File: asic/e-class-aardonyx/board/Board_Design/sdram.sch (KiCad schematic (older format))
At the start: 30 parts, among them J4 Conn_1x4, U15 SKT32E, U2 IS42S32160F-TSOP2, U3 CDCE913PW, Y2 27MHz

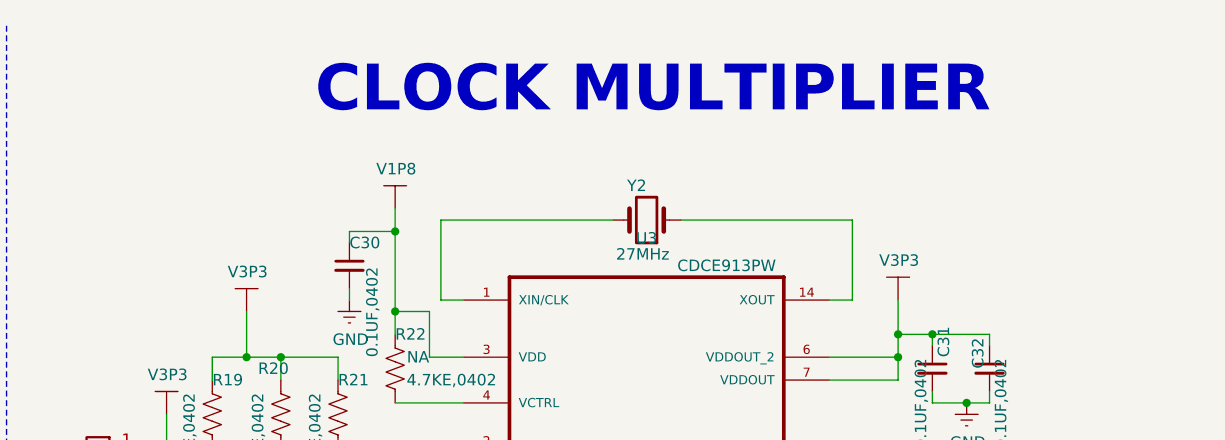
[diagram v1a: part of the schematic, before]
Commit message: Adding capacitors to clock
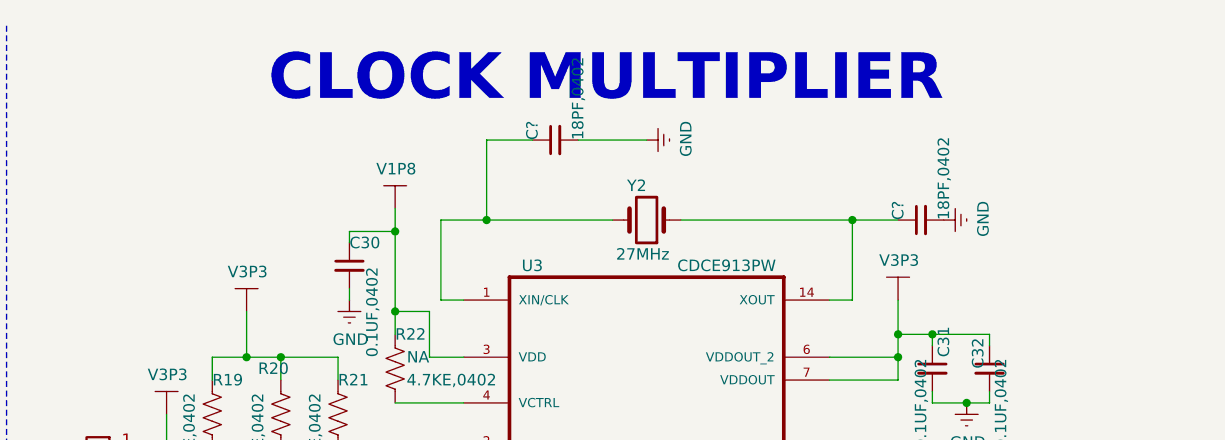
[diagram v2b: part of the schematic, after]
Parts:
- added C? (x2): 18PF,0402, Capacitor_SMD:C_0402_1005Metric, symbol Aardonyx-rescue:C_Small-aardonyx
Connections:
- net GNDREF: now also C?.2, C?.2
- net at U3.1 (XIN/CLK), Y2.2: now also C?.1
- net at U3.14 (XOUT), Y2.1: now also C?.1
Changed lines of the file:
@@
 Text Label 10200 2600 0    50   ~ 0
 CLK
-Text Notes 7300 900  0    200  ~ 40
+Text Notes 10050 850  2    200  ~ 40
 CLOCK MULTIPLIER\n
 Wire Wire Line
-	8600 1350 7850 1350
+	8600 1350 8050 1350
 Wire Wire Line
 	7850 1350 7850 1700
@@
 AR Path="/5ED5EB9F" Ref="U3"  Part="1"
 AR Path="/5D8B37B8/5ED5EB9F" Ref="U3"  Part="1"
-F 0 "U3" H 8750 2970 50  0000 C CNN
+F 0 "U3" H 8250 2850 50  0000 C CNN
 F 1 "CDCE913PW" H 9100 2850 50  0000 C CNN
 F 2 "Package_SO:TSSOP-14_4.4x5mm_P0.65mm" H 8900 2000 50  0001 L BNN
@@
 	7650 1400 7650 1300
 Connection ~ 7650 1400
+$Comp
+L Aardonyx-rescue:C_Small-aardonyx C?
+U 1 1 5F202590
+P 9950 1350
+F 0 "C?" H 9950 1450 50  0000 L CNN
+F 1 "18PF,0402" H 9950 1250 50  0000 L CNN
+F 2 "Capacitor_SMD:C_0402_1005Metric" H 9950 1350 50  0001 C CNN
+F 3 "https://www.digikey.in/product-detail/en/yageo/CC0201JRNPO9BN180/311-1386-1-ND/2833692" H 9950 1350 50  0001 C CNN
+F 4 "311-1386-1-ND " H 9950 1350 50  0001 C CNN "Digikey PartNumber"
+F 5 "CAP CER 18PF 50V C0G/NPO 0201 " H 9950 1350 50  0001 C CNN "Description"
+F 6 "CC0201JRNPO9BN180 " H 9950 1350 50  0001 C CNN "Manufactured Part Number"
+F 7 "Yageo" H 9950 1350 50  0001 C CNN "Maufaturer"
+	1    9950 1350
+	0    -1   -1   0
+$EndComp
+Wire Wire Line
+	9850 1350 9650 1350
+Connection ~ 9650 1350
+$Comp
+L Aardonyx-rescue:GND-aardonyx #PWR?
+U 1 1 5F21B9C6
+P 10050 1350
+AR Path="/5D8B3740/5F21B9C6" Ref="#PWR?"  Part="1"
+AR Path="/5D8B37B8/5F21B9C6" Ref="#PWR?"  Part="1"
+F 0 "#PWR?" H 10050 1100 50  0001 C CNN
+F 1 "GND" H 10055 1177 50  0000 C CNN
+F 2 "" H 10050 1350 50  0001 C CNN
+F 3 "" H 10050 1350 50  0001 C CNN
+	1    10050 1350
+	0    -1   -1   0
+$EndComp
+$Comp
+L Aardonyx-rescue:C_Small-aardonyx C?
+U 1 1 5F229012
+P 8350 1000
+F 0 "C?" H 8350 1100 50  0000 L CNN
+F 1 "18PF,0402" H 8350 900 50  0000 L CNN
+F 2 "Capacitor_SMD:C_0402_1005Metric" H 8350 1000 50  0001 C CNN
+F 3 "https://www.digikey.in/product-detail/en/yageo/CC0201JRNPO9BN180/311-1386-1-ND/2833692" H 8350 1000 50  0001 C CNN
+F 4 "311-1386-1-ND " H 8350 1000 50  0001 C CNN "Digikey PartNumber"
+F 5 "CAP CER 18PF 50V C0G/NPO 0201 " H 8350 1000 50  0001 C CNN "Description"
+F 6 "CC0201JRNPO9BN180 " H 8350 1000 50  0001 C CNN "Manufactured Part Number"
+F 7 "Yageo" H 8350 1000 50  0001 C CNN "Maufaturer"
+	1    8350 1000
+	0    -1   -1   0
+$EndComp
+Wire Wire Line
+	8250 1000 8050 1000
+Wire Wire Line
+	8750 1000 8450 1000
+$Comp
+L Aardonyx-rescue:GND-aardonyx #PWR?
+U 1 1 5F24315B
+P 8750 1000
+AR Path="/5D8B3740/5F24315B" Ref="#PWR?"  Part="1"
+AR Path="/5D8B37B8/5F24315B" Ref="#PWR?"  Part="1"
+F 0 "#PWR?" H 8750 750 50  0001 C CNN
+F 1 "GND" H 8755 827 50  0000 C CNN
+F 2 "" H 8750 1000 50  0001 C CNN
+F 3 "" H 8750 1000 50  0001 C CNN
+	1    8750 1000
+	0    -1   -1   0
+$EndComp
+Wire Wire Line
+	8050 1000 8050 1350
 Wire Bus Line
 	1550 5700 1550 6100
@@
 Wire Bus Line
 	4650 3000 4650 6600
+Connection ~ 8050 1350
+Wire Wire Line
+	8050 1350 7850 1350
 $EndSCHEMATC

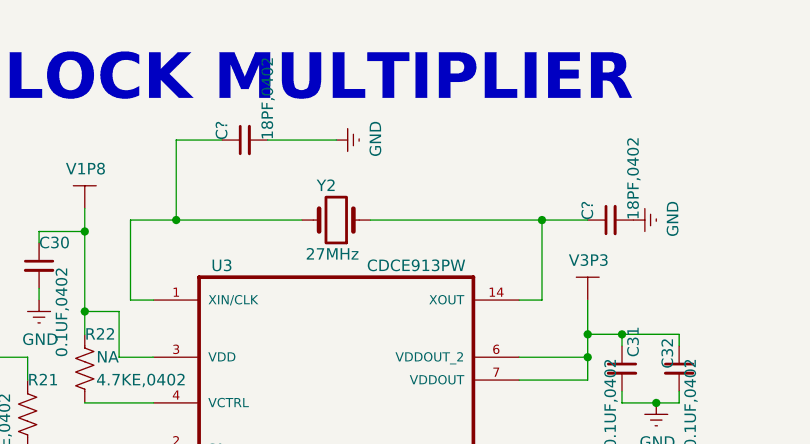
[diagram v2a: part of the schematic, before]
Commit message: updated footprint c37 & f1
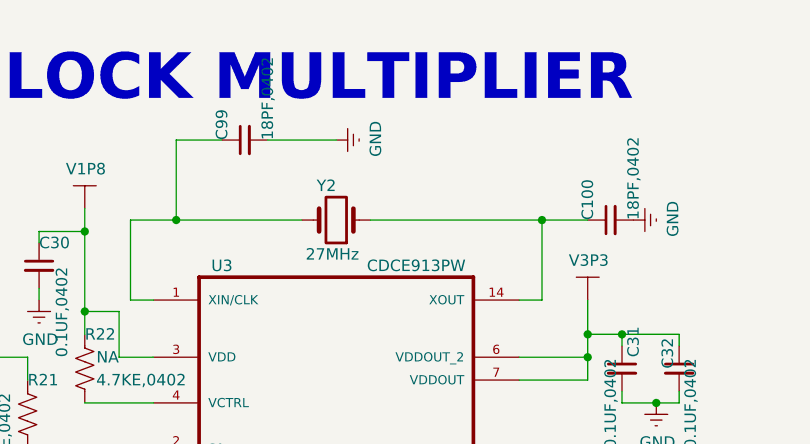
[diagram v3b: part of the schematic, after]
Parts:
- gave numbers to parts that had none: 2
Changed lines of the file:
@@
 Connection ~ 7650 1400
 $Comp
-L Aardonyx-rescue:C_Small-aardonyx C?
+L Aardonyx-rescue:C_Small-aardonyx C100
 U 1 1 5F202590
 P 9950 1350
-F 0 "C?" H 9950 1450 50  0000 L CNN
+F 0 "C100" H 9950 1450 50  0000 L CNN
 F 1 "18PF,0402" H 9950 1250 50  0000 L CNN
 F 2 "Capacitor_SMD:C_0402_1005Metric" H 9950 1350 50  0001 C CNN
@@
 P 10050 1350
 AR Path="/5D8B3740/5F21B9C6" Ref="#PWR?"  Part="1"
-AR Path="/5D8B37B8/5F21B9C6" Ref="#PWR?"  Part="1"
-F 0 "#PWR?" H 10050 1100 50  0001 C CNN
+AR Path="/5D8B37B8/5F21B9C6" Ref="#PWR0186"  Part="1"
+F 0 "#PWR0186" H 10050 1100 50  0001 C CNN
 F 1 "GND" H 10055 1177 50  0000 C CNN
 F 2 "" H 10050 1350 50  0001 C CNN
@@
 $EndComp
 $Comp
-L Aardonyx-rescue:C_Small-aardonyx C?
+L Aardonyx-rescue:C_Small-aardonyx C99
 U 1 1 5F229012
 P 8350 1000
-F 0 "C?" H 8350 1100 50  0000 L CNN
+F 0 "C99" H 8350 1100 50  0000 L CNN
 F 1 "18PF,0402" H 8350 900 50  0000 L CNN
 F 2 "Capacitor_SMD:C_0402_1005Metric" H 8350 1000 50  0001 C CNN
@@
 P 8750 1000
 AR Path="/5D8B3740/5F24315B" Ref="#PWR?"  Part="1"
-AR Path="/5D8B37B8/5F24315B" Ref="#PWR?"  Part="1"
-F 0 "#PWR?" H 8750 750 50  0001 C CNN
+AR Path="/5D8B37B8/5F24315B" Ref="#PWR0232"  Part="1"
+F 0 "#PWR0232" H 8750 750 50  0001 C CNN
 F 1 "GND" H 8755 827 50  0000 C CNN
 F 2 "" H 8750 1000 50  0001 C CNN
@@
 Wire Wire Line
 	8050 1000 8050 1350
+Connection ~ 8050 1350
+Wire Wire Line
+	8050 1350 7850 1350
 Wire Bus Line
 	1550 5700 1550 6100
@@
 Wire Bus Line
 	4650 3000 4650 6600
-Connection ~ 8050 1350
-Wire Wire Line
-	8050 1350 7850 1350
 $EndSCHEMATC

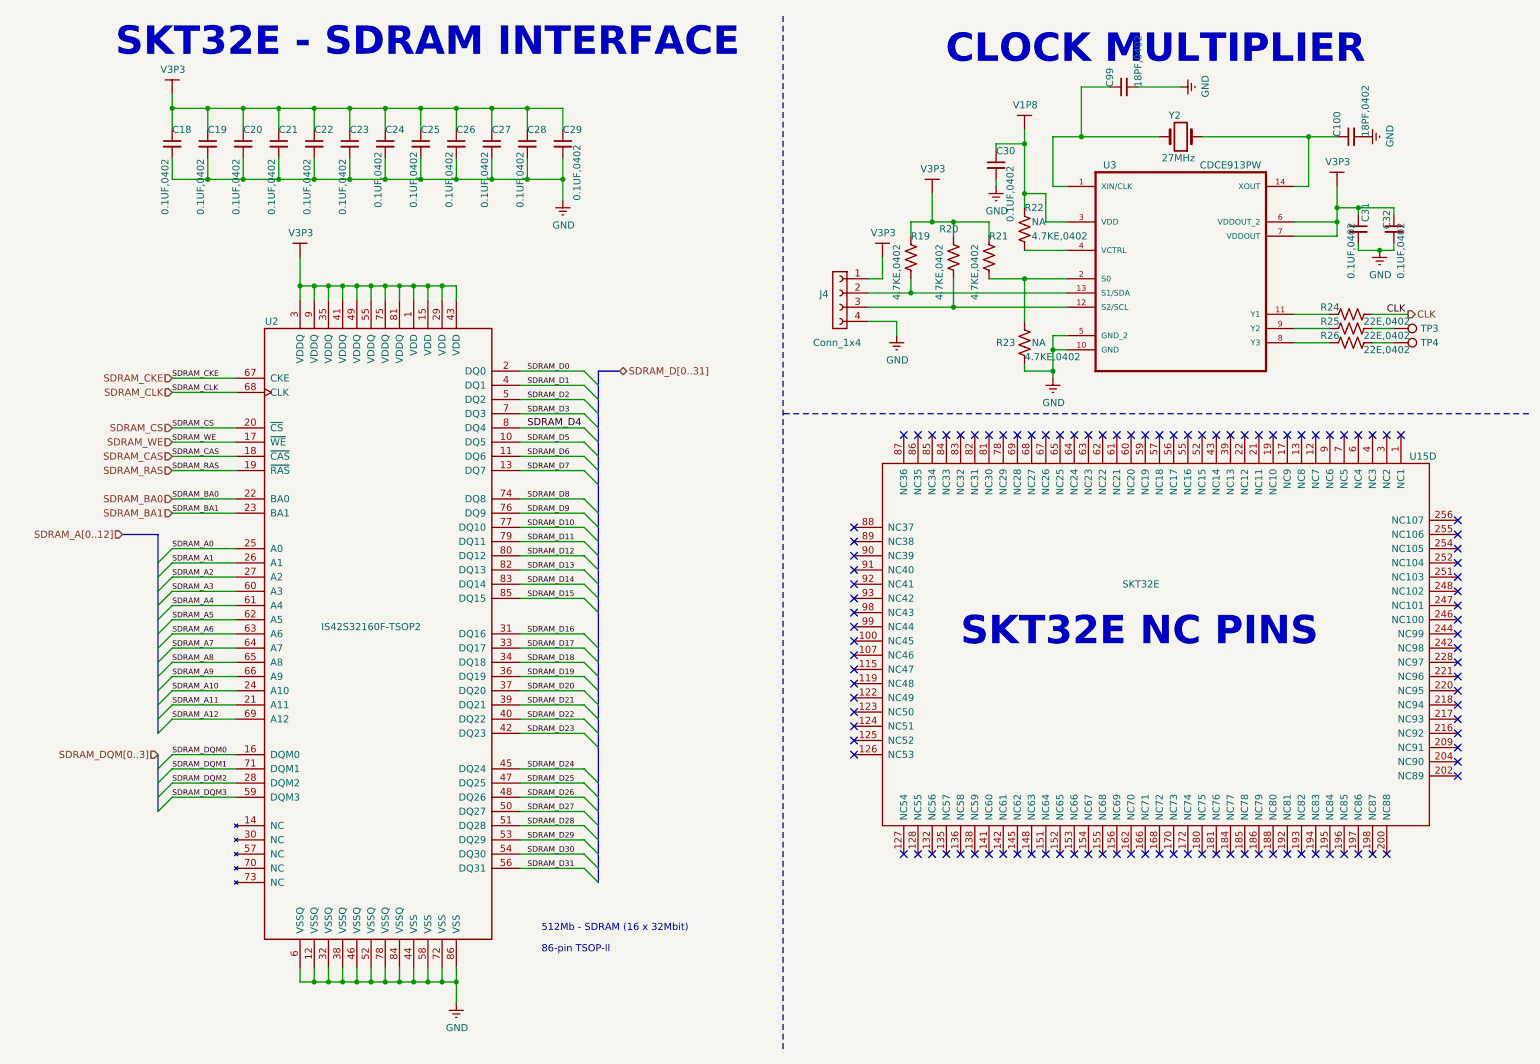
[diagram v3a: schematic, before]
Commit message: Updating layout after back annotation
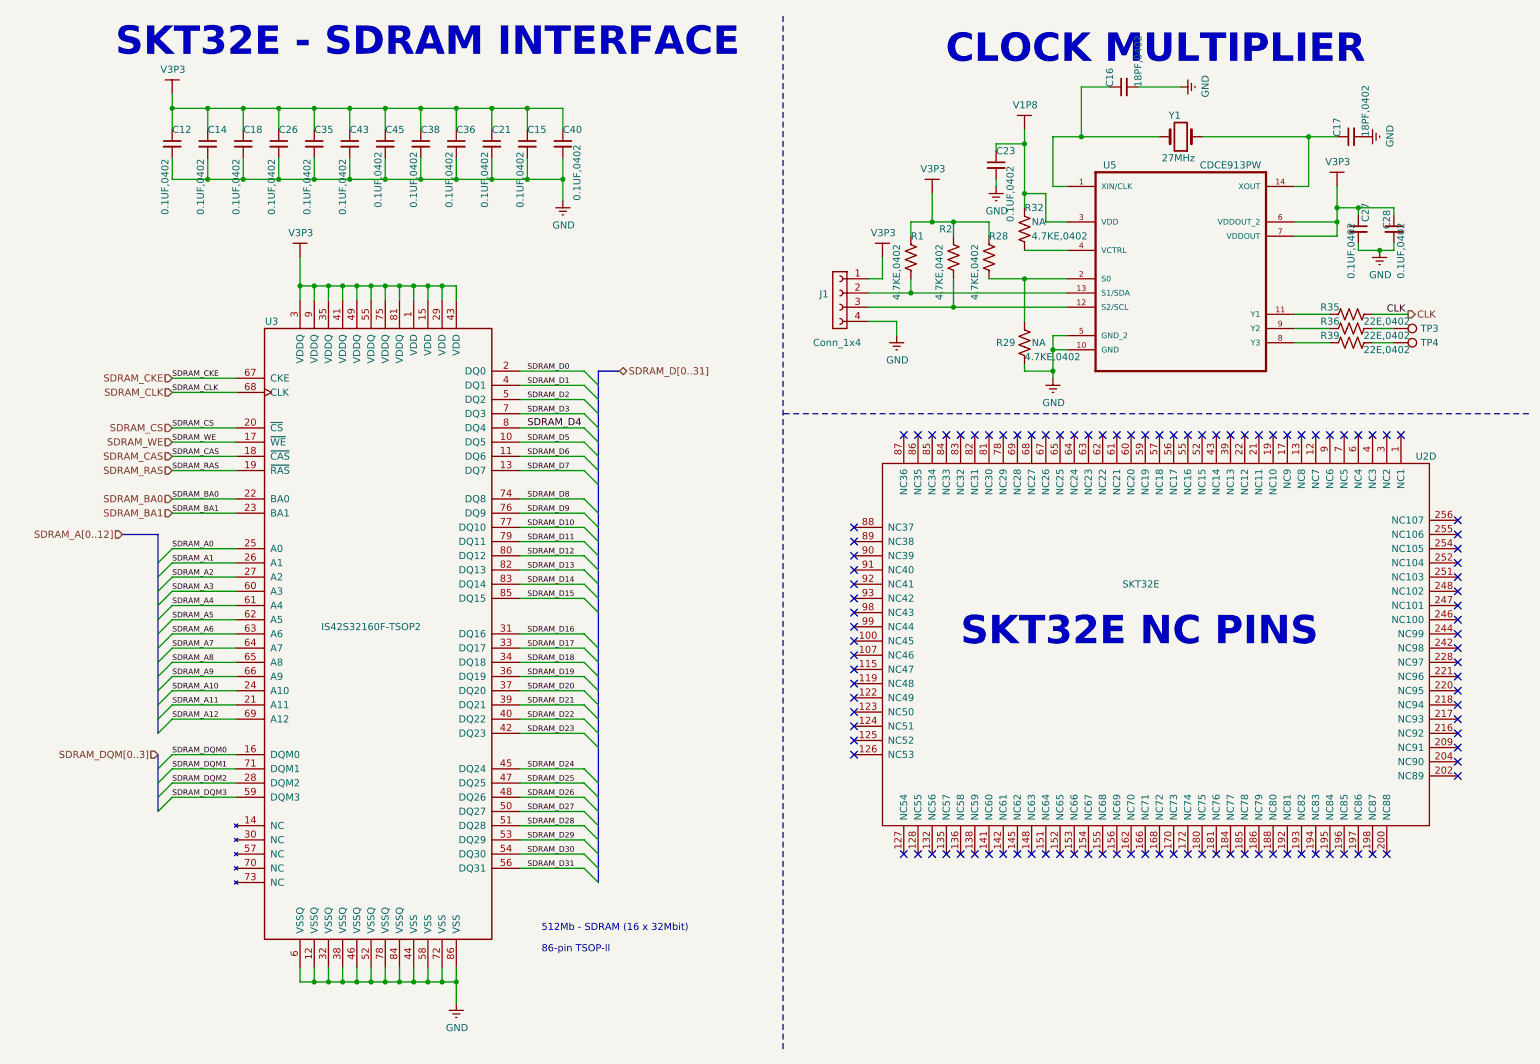
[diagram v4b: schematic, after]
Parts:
- renumbered C18 to C12, C19 to C14, C28 to C15, C99 to C16, C100 to C17, C20 to C18, C27 to C21, C30 to C23, C21 to C26, C31 to C27, C32 to C28, C22 to C35, C26 to C36, C25 to C38, C29 to C40, C23 to C43, C24 to C45, J4 to J1, R19 to R1, R20 to R2, R21 to R28, R23 to R29, R22 to R32, R24 to R35, R25 to R36, R26 to R39, U15 to U2, U2 to U3, Y2 to Y1
